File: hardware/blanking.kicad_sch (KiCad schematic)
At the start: 21 parts

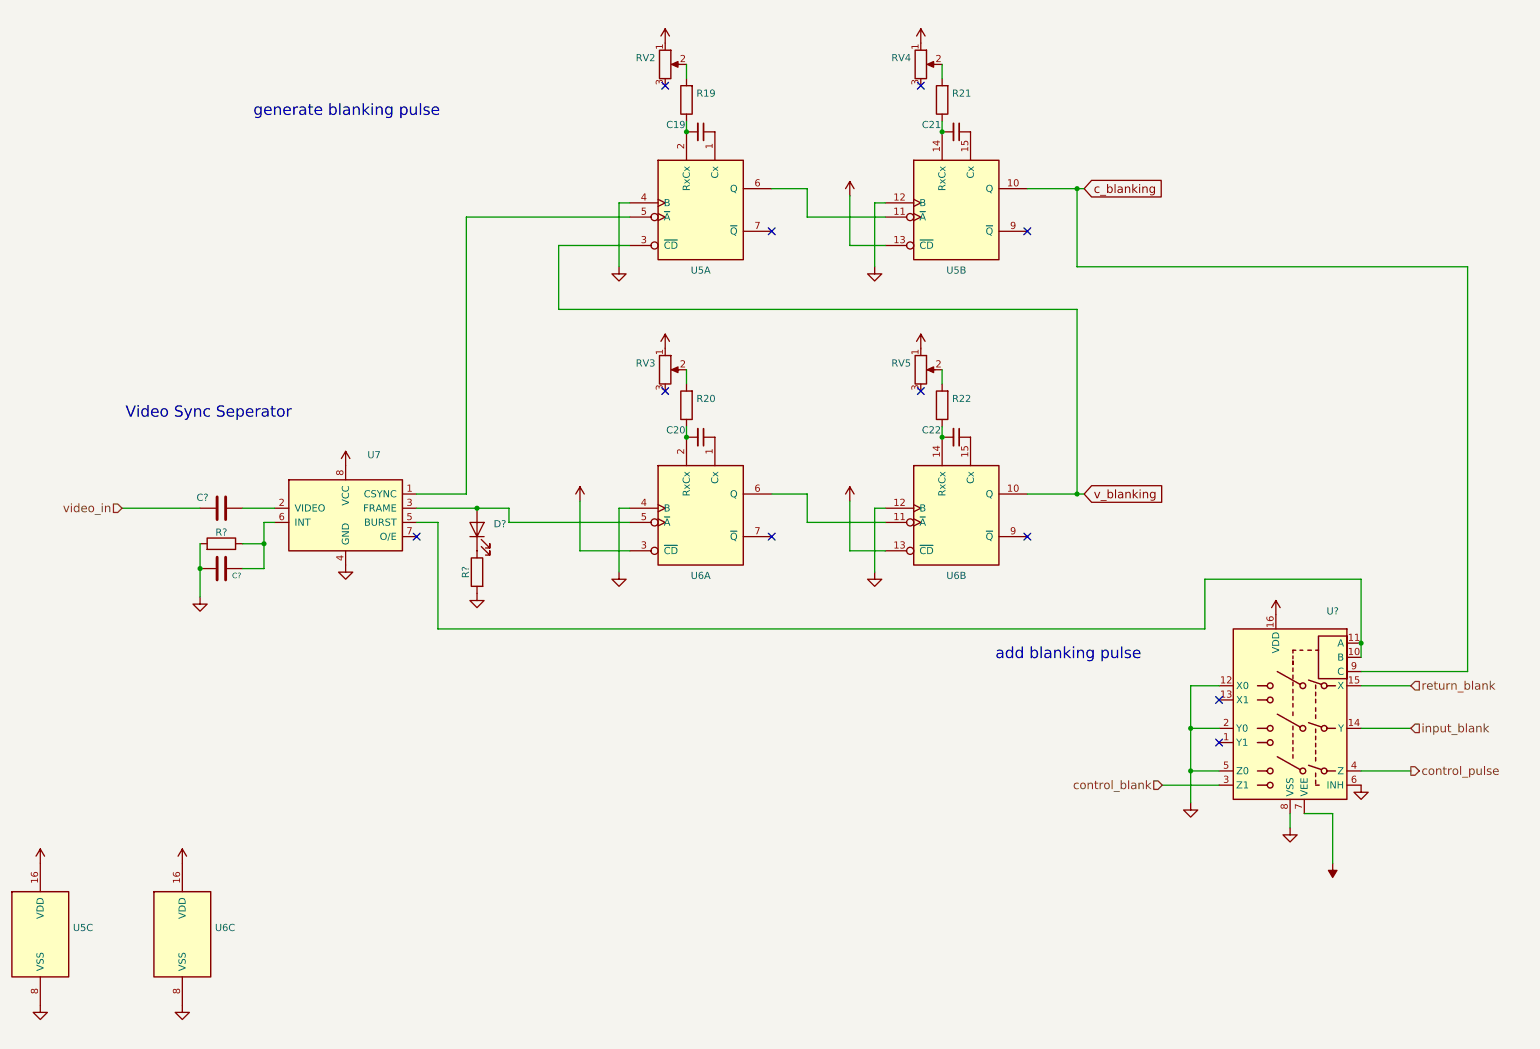
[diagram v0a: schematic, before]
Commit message: update blanking values
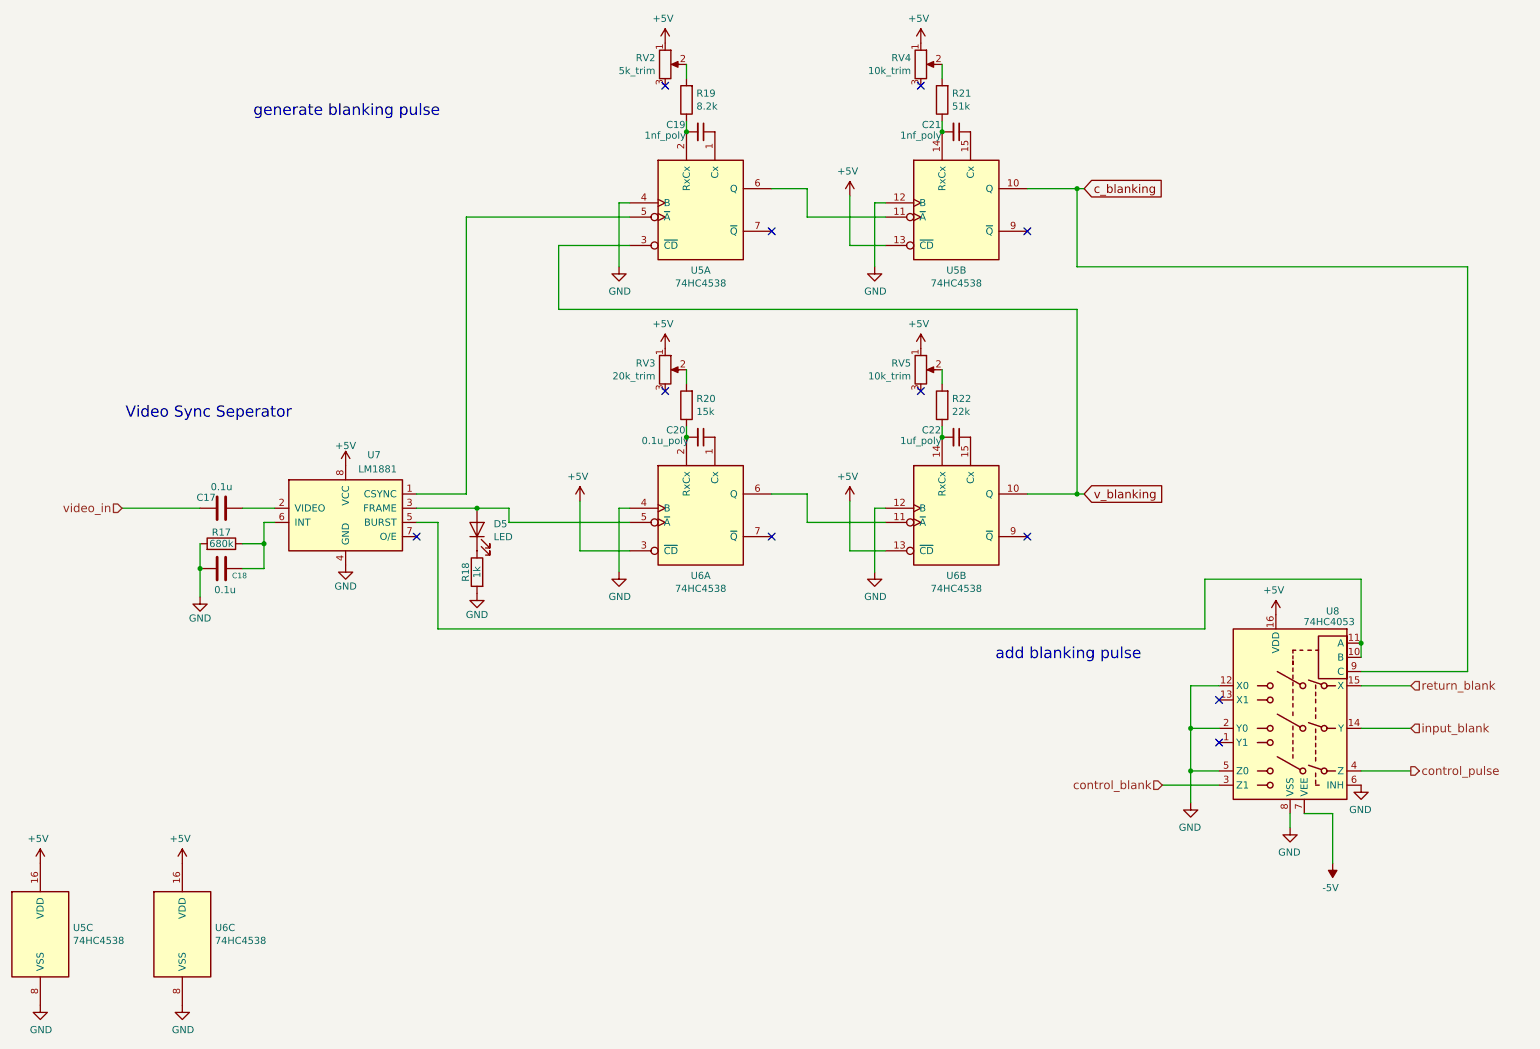
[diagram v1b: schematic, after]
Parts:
- C17, C18: renamed from C?; value (none) -> 0.1u; footprint (none) -> Capacitor_THT:C_Disc_D4.3mm_W1.9mm_P5.00mm
- C19, C21: value (none) -> 1nf_poly; footprint (none) -> Capacitor_THT:C_Disc_D4.3mm_W1.9mm_P5.00mm
- C20: value (none) -> 0.1u_poly; footprint (none) -> Capacitor_THT:C_Disc_D4.3mm_W1.9mm_P5.00mm
- C22: value (none) -> 1uf_poly; footprint (none) -> Capacitor_THT:C_Disc_D4.3mm_W1.9mm_P5.00mm
- D5: renamed from D?; value (none) -> LED; footprint (none) -> LED_THT:LED_D3.0mm
- R17: renamed from R?; value (none) -> 680k; footprint (none) -> Resistor_THT:R_Axial_DIN0204_L3.6mm_D1.6mm_P7.62mm_Horizontal
- R18: renamed from R?; value (none) -> 1k; footprint (none) -> Resistor_THT:R_Axial_DIN0204_L3.6mm_D1.6mm_P7.62mm_Horizontal
- R19: value (none) -> 8.2k; footprint (none) -> Resistor_THT:R_Axial_DIN0204_L3.6mm_D1.6mm_P7.62mm_Horizontal
- R20: value (none) -> 15k; footprint (none) -> Resistor_THT:R_Axial_DIN0204_L3.6mm_D1.6mm_P7.62mm_Horizontal
- R21: value (none) -> 51k; footprint (none) -> Resistor_THT:R_Axial_DIN0204_L3.6mm_D1.6mm_P7.62mm_Horizontal
- R22: value (none) -> 22k; footprint (none) -> Resistor_THT:R_Axial_DIN0204_L3.6mm_D1.6mm_P7.62mm_Horizontal
- RV2: value (none) -> 5k_trim; footprint (none) -> lib_fp:tht_vertical_trim_3362
- RV3: value (none) -> 20k_trim; footprint (none) -> lib_fp:tht_vertical_trim_3362
- RV4, RV5: value (none) -> 10k_trim; footprint (none) -> lib_fp:tht_vertical_trim_3362
- U5, U6: value (none) -> 74HC4538; footprint (none) -> Package_DIP:DIP-16_W7.62mm_LongPads
- U7: value (none) -> LM1881; footprint (none) -> lib_fp:DIP-SOIC-8
- U8: renamed from U?; value (none) -> 74HC4053; footprint (none) -> Package_DIP:DIP-16_W7.62mm_LongPads

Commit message: tweak values for blanking
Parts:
- R19: value 8.2k -> 10k
- R21: value 51k -> 68k
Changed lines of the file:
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@@
       (effects (font (size 1.27 1.27)) (justify right))
     )
-    (property "Value" "8.2k" (id 1) (at 138.938 29.718 0)
+    (property "Value" "10k" (id 1) (at 138.938 29.718 0)
       (effects (font (size 1.27 1.27)) (justify right))
     )
@@
       (effects (font (size 1.27 1.27)) (justify right))
     )
-    (property "Value" "51k" (id 1) (at 184.658 29.718 0)
+    (property "Value" "68k" (id 1) (at 184.658 29.718 0)
       (effects (font (size 1.27 1.27)) (justify right))
     )

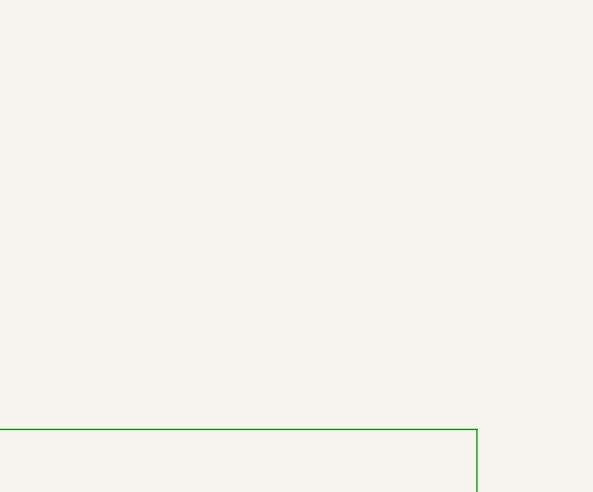
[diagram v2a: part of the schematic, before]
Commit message: create revision for new power circuit
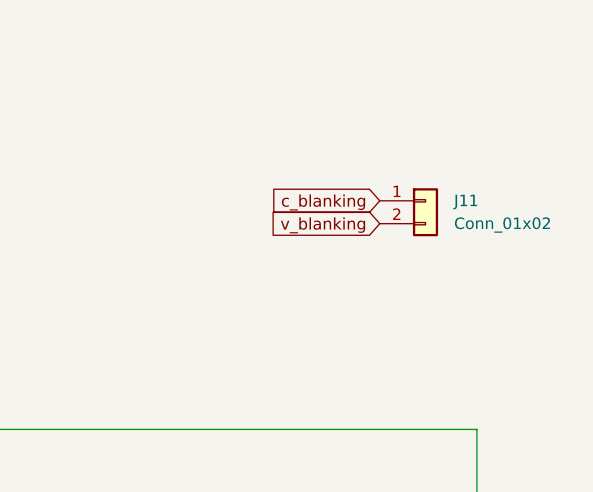
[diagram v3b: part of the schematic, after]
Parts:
- added J11: Conn_01x02, Connector_PinHeader_2.54mm:PinHeader_1x02_P2.54mm_Vertical, symbol Connector_Generic:Conn_01x02
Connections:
- net c_blanking: now also J11.1 (Pin_1)
- net v_blanking: now also J11.2 (Pin_2)
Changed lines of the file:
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@@
+    )
+  )
+  (global_label "v_blanking" (shape input) (at 266.065 35.56 180) (fields_autoplaced)
+    (effects (font (size 1.3 1.3)) (justify right))
+    (property "Intersheet References" "${INTERSHEET_REFS}" (id 0) (at 253.4717 35.4788 0)
+      (effects (font (size 1.3 1.3)) (justify right) hide)
+    )
+  )
+  (global_label "c_blanking" (shape input) (at 266.065 33.02 180) (fields_autoplaced)
+    (effects (font (size 1.3 1.3)) (justify right))
+    (property "Intersheet References" "${INTERSHEET_REFS}" (id 0) (at 253.3479 32.9388 0)
+      (effects (font (size 1.3 1.3)) (justify right) hide)
     )
   )
@@
     (pin "1")
   )
+  (symbol (lib_id "Connector_Generic:Conn_01x02") (at 271.145 33.02 0) (unit 1)
+    (in_bom yes) (on_board yes) (fields_autoplaced)
+    (property "Reference" "J11" (id 0) (at 274.32 33.0199 0)
+      (effects (font (size 1.27 1.27)) (justify left))
+    )
+    (property "Value" "Conn_01x02" (id 1) (at 274.32 35.5599 0)
+      (effects (font (size 1.27 1.27)) (justify left))
+    )
+    (property "Footprint" "Connector_PinHeader_2.54mm:PinHeader_1x02_P2.54mm_Vertical" (id 2) (at 271.145 33.02 0)
+      (effects (font (size 1.27 1.27)) hide)
+    )
+    (property "Datasheet" "~" (id 3) (at 271.145 33.02 0)
+      (effects (font (size 1.27 1.27)) hide)
+    )
+    (pin "1")
+    (pin "2")
+  )
 )

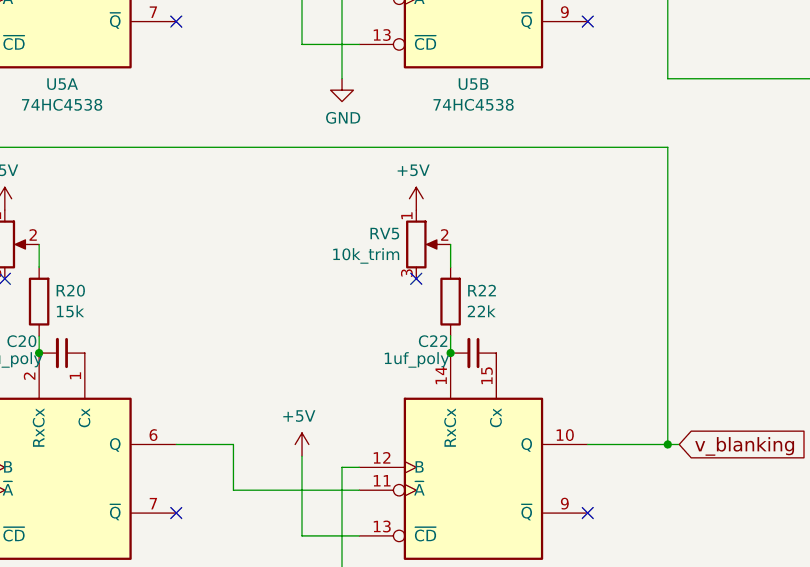
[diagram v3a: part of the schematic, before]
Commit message: update to v1_0_1 to increase range of blanking trim
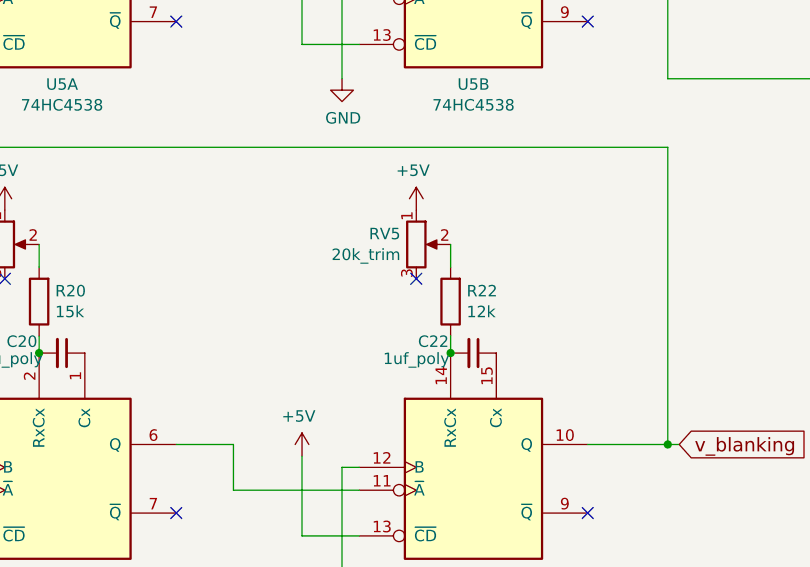
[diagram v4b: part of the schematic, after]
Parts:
- R22: value 22k -> 12k
- RV5: value 10k_trim -> 20k_trim
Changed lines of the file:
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@@
       (effects (font (size 1.27 1.27)) (justify right))
     )
-    (property "Value" "22k" (id 1) (at 184.658 84.328 0)
+    (property "Value" "12k" (id 1) (at 184.658 84.328 0)
       (effects (font (size 1.27 1.27)) (justify right))
     )
@@
       (effects (font (size 1.27 1.27)) (justify right))
     )
-    (property "Value" "10k_trim" (id 1) (at 177.3174 77.978 0)
+    (property "Value" "20k_trim" (id 1) (at 177.3174 77.978 0)
       (effects (font (size 1.27 1.27)) (justify right))
     )
